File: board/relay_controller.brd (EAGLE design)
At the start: 75 x 50 mm, 73 parts, among them IC1 STM32F103C8T, IC3 AT24C, X1 RJ45-8L21-S, X2 RJ45-8L21-S

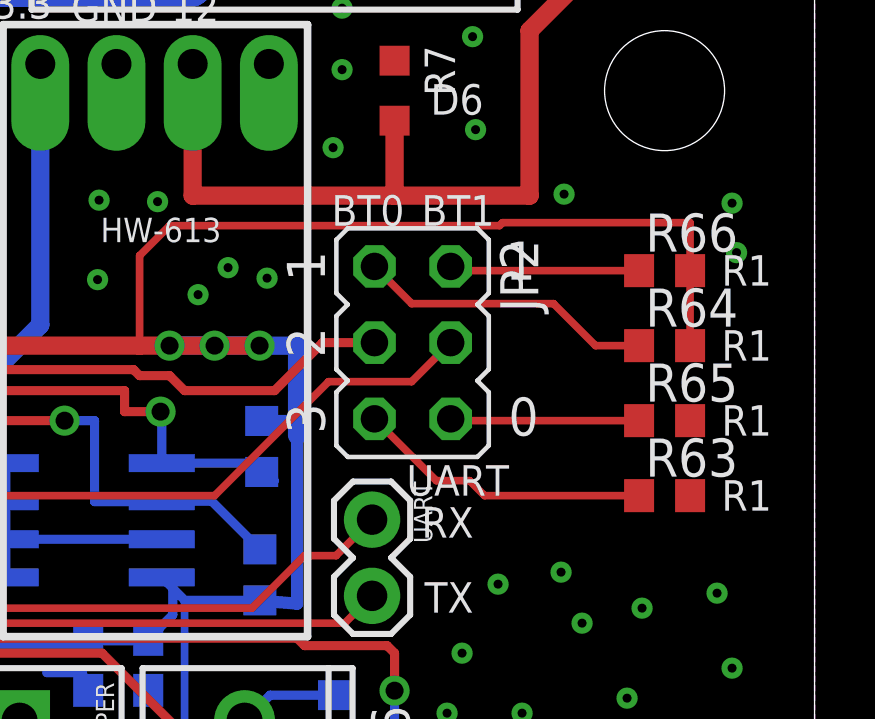
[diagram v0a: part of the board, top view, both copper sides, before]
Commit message: change to solderable boot jumper
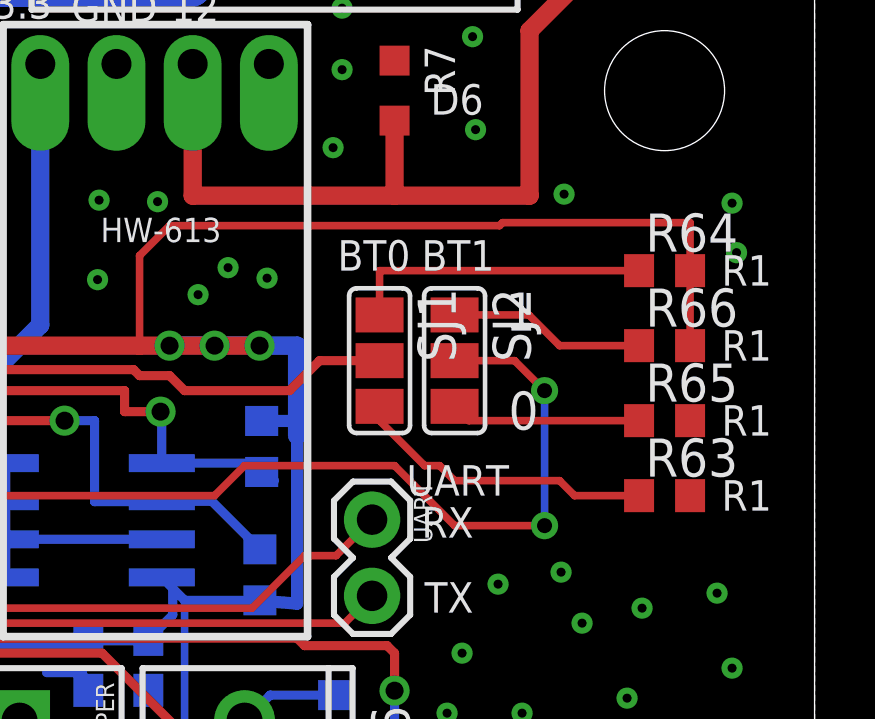
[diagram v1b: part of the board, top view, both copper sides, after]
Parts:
- removed JP2: (no value), jumper:JP3Q
- added SJ1, SJ2: (no value), jumper:SJ_2
- moved R64 2.50 mm to (70.0, 31.5)
- moved R66 2.50 mm to (70.0, 29.0)
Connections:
- net BOOT0: now also SJ1.2; no longer JP2.3
- net BOOT1: now also SJ2.2; no longer JP2.4
- net N$29: now also SJ2.1; no longer JP2.2
- net N$30: now also SJ1.1; no longer JP2.1
- net N$31: now also SJ2.3; no longer JP2.6
- net N$32: now also SJ1.3; no longer JP2.5
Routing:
- net BOOT1: track 46.0 -> 56.1 mm, vias 2 -> 4
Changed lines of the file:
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@@
 <text x="61.9" y="22.6" size="1.016" layer="121">RX</text>
 <text x="62" y="20.1" size="1.016" layer="121">TX</text>
-<text x="58.9" y="33" size="1.016" layer="121">BT0</text>
-<text x="61.9" y="33" size="1.016" layer="121">BT1</text>
-<text x="64.8" y="26" size="1.27" layer="121">0</text>
-<text x="64.7" y="31.2" size="1.27" layer="121">1</text>
+<text x="59.1" y="31.5" size="1.016" layer="121">BT0</text>
+<text x="61.9" y="31.5" size="1.016" layer="121">BT1</text>
+<text x="64.8" y="26.2" size="1.27" layer="121">0</text>
+<text x="64.7" y="29.5" size="1.27" layer="121">1</text>
 <text x="71.9" y="28.5" size="1.016" layer="121">R1</text>
 <text x="71.9" y="26" size="1.016" layer="121">R1</text>
@@
 <element name="U$5" library="mounting" package="C45-DIN-MOUNT-2-HOLE" value="" x="5" y="25"/>
 <element name="R63" library="rcl" package="R0603" value="10k" x="70" y="24"/>
-<element name="R64" library="rcl" package="R0603" value="10k" x="70" y="29"/>
+<element name="R64" library="rcl" package="R0603" value="10k" x="70" y="31.5"/>
 <element name="R65" library="rcl" package="R0603" value="10k" x="70" y="26.5"/>
-<element name="R66" library="rcl" package="R0603" value="10k" x="70" y="31.5"/>
-<element name="JP2" library="jumper" package="JP3Q" value="" x="61.6" y="29.1" rot="R270"/>
+<element name="R66" library="rcl" package="R0603" value="10k" x="70" y="29"/>
+<element name="SJ1" library="jumper" package="SJ_2" value="" x="60.5" y="28.5" rot="R270"/>
+<element name="SJ2" library="jumper" package="SJ_2" value="" x="63" y="28.5" rot="R270"/>
 </elements>
 <signals>
@@
 <wire x1="39.5" y1="24.5" x2="44.5" y2="24.5" width="0.6096" layer="16"/>
 <wire x1="44.5" y1="19" x2="44.5" y2="24.5" width="0.6096" layer="16"/>
-<wire x1="70.85" y1="29" x2="70.85" y2="31.5" width="0.254" layer="1"/>
 <wire x1="52.5" y1="29" x2="52.5" y2="32" width="0.254" layer="1"/>
 <wire x1="52.5" y1="32" x2="53.5" y2="33" width="0.254" layer="1"/>
@@
 <wire x1="64.6" y1="33.1" x2="70.85" y2="33.1" width="0.254" layer="1"/>
 <wire x1="70.85" y1="31.5" x2="70.85" y2="33.1" width="0.254" layer="1"/>
+<wire x1="70.85" y1="31.5" x2="70.85" y2="29" width="0.254" layer="1"/>
 </signal>
 <signal name="RELAY_16">
@@
 </signal>
 <signal name="BOOT1">
-<contactref element="JP2" pad="4"/>
 <contactref element="IC1" pad="20"/>
 <wire x1="32.75" y1="15.75" x2="32.75" y2="12.25" width="0.3048" layer="1"/>
 <wire x1="32.75" y1="12.25" x2="33.5" y2="11.5" width="0.3048" layer="1"/>
 <wire x1="33.5" y1="11.5" x2="40.1" y2="11.5" width="0.3048" layer="1"/>
-<wire x1="62.87" y1="29.1" x2="61.57" y2="27.8" width="0.254" layer="1"/>
-<wire x1="61.57" y1="27.8" x2="58.8" y2="27.8" width="0.254" layer="1"/>
-<wire x1="58.8" y1="27.8" x2="55" y2="24" width="0.254" layer="1"/>
 <wire x1="55" y1="24" x2="44.5" y2="24" width="0.254" layer="1"/>
 <wire x1="44.5" y1="24" x2="42.5" y2="22" width="0.254" layer="1"/>
@@
 <via x="40.9" y="12.3" extent="1-16" drill="0.5"/>
 <wire x1="40.9" y1="12.3" x2="40.1" y2="11.5" width="0.3048" layer="1"/>
+<contactref element="SJ2" pad="2"/>
+<wire x1="63" y1="28.5" x2="65" y2="28.5" width="0.254" layer="1"/>
+<wire x1="65" y1="28.5" x2="66" y2="27.5" width="0.254" layer="1"/>
+<via x="66" y="27.5" extent="1-16" drill="0.5"/>
+<wire x1="66" y1="27.5" x2="66" y2="23" width="0.254" layer="16"/>
+<via x="66" y="23" extent="1-16" drill="0.5"/>
+<wire x1="66" y1="23" x2="63" y2="23" width="0.254" layer="1"/>
+<wire x1="63" y1="23" x2="61" y2="25" width="0.254" layer="1"/>
+<wire x1="61" y1="25" x2="56" y2="25" width="0.254" layer="1"/>
+<wire x1="56" y1="25" x2="55" y2="24" width="0.254" layer="1"/>
 </signal>
 <signal name="BOOT0">
-<contactref element="JP2" pad="3"/>
 <contactref element="IC1" pad="44"/>
 <wire x1="31.25" y1="24.25" x2="31.25" y2="32.5" width="0.3048" layer="1"/>
@@
 <wire x1="52.5" y1="28" x2="53.5" y2="28" width="0.3048" layer="1"/>
 <wire x1="53.5" y1="28" x2="54" y2="27.5" width="0.3048" layer="1"/>
-<wire x1="54" y1="27.5" x2="57" y2="27.5" width="0.3048" layer="1"/>
-<wire x1="57" y1="27.5" x2="58.6" y2="29.1" width="0.3048" layer="1"/>
-<wire x1="58.6" y1="29.1" x2="60.33" y2="29.1" width="0.3048" layer="1"/>
+<wire x1="54" y1="27.5" x2="57.5" y2="27.5" width="0.3048" layer="1"/>
+<contactref element="SJ1" pad="2"/>
+<wire x1="57.5" y1="27.5" x2="58.5" y2="28.5" width="0.3048" layer="1"/>
+<wire x1="58.5" y1="28.5" x2="60.5" y2="28.5" width="0.3048" layer="1"/>
 </signal>
 <signal name="N$29">
 <contactref element="R66" pad="1"/>
-<contactref element="JP2" pad="2"/>
-<wire x1="62.87" y1="31.64" x2="63.01" y2="31.5" width="0.254" layer="1"/>
-<wire x1="63.01" y1="31.5" x2="69.15" y2="31.5" width="0.254" layer="1"/>
+<contactref element="SJ2" pad="1"/>
+<wire x1="63" y1="30.024" x2="65.476" y2="30.024" width="0.254" layer="1"/>
+<wire x1="65.476" y1="30.024" x2="66.5" y2="29" width="0.254" layer="1"/>
+<wire x1="66.5" y1="29" x2="69.15" y2="29" width="0.254" layer="1"/>
 </signal>
 <signal name="N$30">
 <contactref element="R64" pad="1"/>
-<contactref element="JP2" pad="1"/>
-<wire x1="60.33" y1="31.64" x2="61.57" y2="30.4" width="0.254" layer="1"/>
-<wire x1="61.57" y1="30.4" x2="66.3" y2="30.4" width="0.254" layer="1"/>
-<wire x1="66.3" y1="30.4" x2="67.7" y2="29" width="0.254" layer="1"/>
-<wire x1="67.7" y1="29" x2="69.15" y2="29" width="0.254" layer="1"/>
+<contactref element="SJ1" pad="1"/>
+<wire x1="60.5" y1="30.024" x2="60.5" y2="31.5" width="0.254" layer="1"/>
+<wire x1="60.5" y1="31.5" x2="69.15" y2="31.5" width="0.254" layer="1"/>
 </signal>
 <signal name="N$31">
 <contactref element="R65" pad="1"/>
-<contactref element="JP2" pad="6"/>
-<wire x1="62.87" y1="26.56" x2="62.93" y2="26.5" width="0.254" layer="1"/>
-<wire x1="62.93" y1="26.5" x2="69.15" y2="26.5" width="0.254" layer="1"/>
+<contactref element="SJ2" pad="3"/>
+<wire x1="69.15" y1="26.5" x2="63.476" y2="26.5" width="0.254" layer="1"/>
+<wire x1="63.476" y1="26.5" x2="63" y2="26.976" width="0.254" layer="1"/>
 </signal>
 <signal name="N$32">
 <contactref element="R63" pad="1"/>
-<contactref element="JP2" pad="5"/>
-<wire x1="60.33" y1="26.56" x2="62.39" y2="24.5" width="0.254" layer="1"/>
-<wire x1="62.39" y1="24.5" x2="63.5" y2="24.5" width="0.254" layer="1"/>
-<wire x1="63.5" y1="24.5" x2="64" y2="24" width="0.254" layer="1"/>
-<wire x1="64" y1="24" x2="69.15" y2="24" width="0.254" layer="1"/>
+<contactref element="SJ1" pad="3"/>
+<wire x1="69.15" y1="24" x2="67" y2="24" width="0.254" layer="1"/>
+<wire x1="67" y1="24" x2="66.5" y2="24.5" width="0.254" layer="1"/>
+<wire x1="66.5" y1="24.5" x2="63" y2="24.5" width="0.254" layer="1"/>
+<wire x1="63" y1="24.5" x2="62.5" y2="25" width="0.254" layer="1"/>
+<wire x1="62.5" y1="25" x2="62" y2="25" width="0.254" layer="1"/>
+<wire x1="62" y1="25" x2="60.5" y2="26.5" width="0.254" layer="1"/>
+<wire x1="60.5" y1="26.5" x2="60.5" y2="26.976" width="0.254" layer="1"/>
 </signal>
 </signals>

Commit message: value for current limiting resistor
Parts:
- R20: value (none) -> 100
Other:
- board text added: "R9"
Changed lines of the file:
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@@
 <text x="71.9" y="23.5" size="1.016" layer="121">R1</text>
 <text x="71.9" y="31" size="1.016" layer="121">R1</text>
+<text x="8.85" y="5.1" size="1.016" layer="122" rot="MR180">R9</text>
 </plain>
 <attributes>
@@
 <element name="R18" library="resistor" package="R0603" value="" x="29.8" y="4.5" rot="MR180"/>
 <element name="R19" library="resistor" package="R0603" value="" x="26.3" y="4.5" rot="MR180"/>
-<element name="R20" library="resistor" package="R0603" value="" x="12.3" y="4.5" rot="MR180"/>
+<element name="R20" library="resistor" package="R0603" value="100" x="12.3" y="4.5" rot="MR180"/>
 <element name="R21" library="resistor" package="R0603" value="" x="15.8" y="4.5" rot="MR0"/>
 <element name="R22" library="resistor" package="R0603" value="" x="22.8" y="4.5" rot="MR180"/>

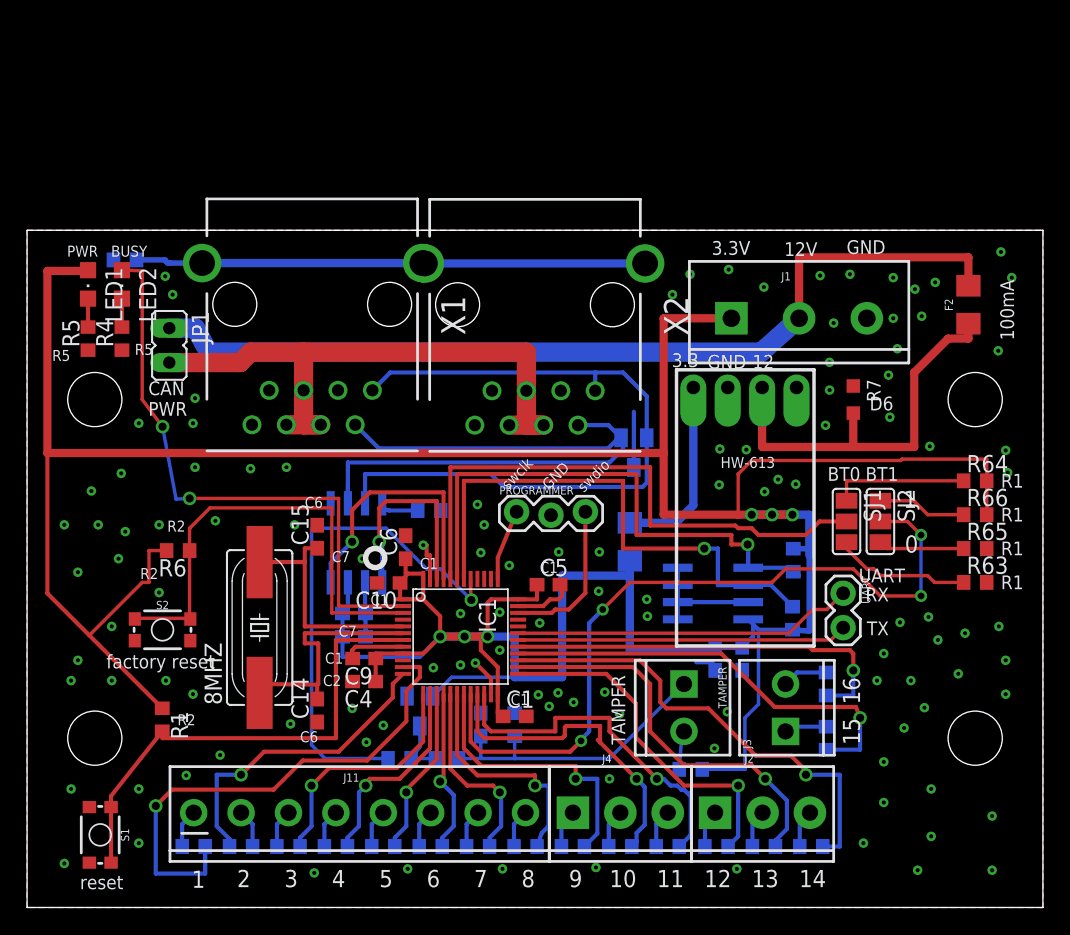
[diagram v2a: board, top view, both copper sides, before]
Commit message: change 16 driver pin to 5 relay output (g6k-2f-y)
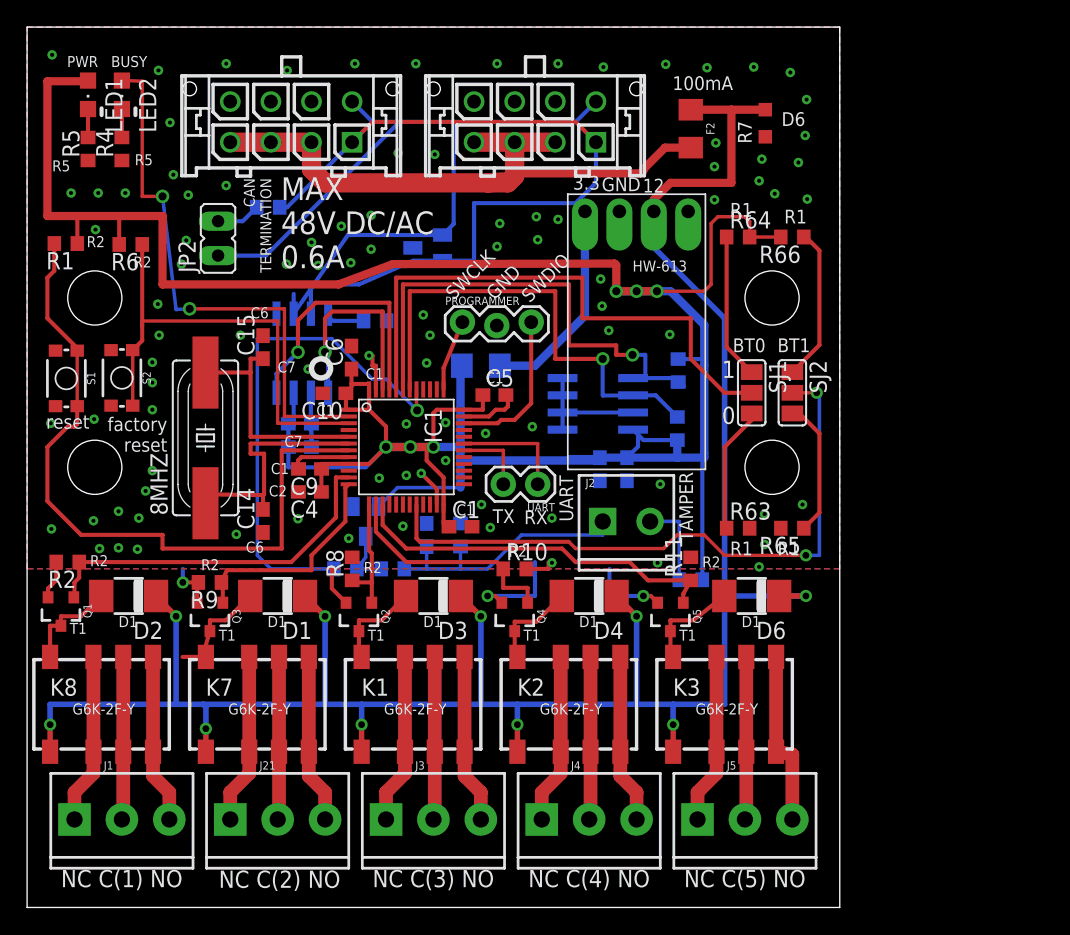
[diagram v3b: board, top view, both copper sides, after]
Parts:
- removed J11: (no value), SparkFun-Connectors:SCREWTERMINAL-3.5MM-8
- removed JP1: (no value), jumper:JP1
- removed R12, R13, R14, R15, R16, R17, R18, R19, R21, R22, R23: (no value), resistor:R0603
- removed R20: 100, resistor:R0603
- removed TAMPER: (no value), SparkFun-Connectors:SCREWTERMINAL-3.5MM-2
- removed U$4, U$5: (no value), mounting:C45-DIN-MOUNT-2-HOLE
- removed X1, X2: RJ45-8L21-S, con-tycoelectronics:RJ45-SHIELD1
- added D1, D2, D3, D4, D6: (no value), diode:DO-214AC
- added J21, J5: (no value), SparkFun-Connectors:SCREWTERMINAL-3.5MM-3
- added JP2: (no value), jumper:JP1
- added K1, K2, K3, K7, K8: G6K-2F-Y, relay:G6K-2F-Y
- added Q1, Q2, Q3, Q4, Q5: 220mA/50V/3.5Ω, SparkFun-DiscreteSemi:SOT23-3
- added R2: 10k, rcl:R0603
- added U$2, U$3: (no value), mounting:C45-DIN-MOUNT-2-HOLE-B
- added X3, X4: (no value), con-molex-micro-fit-3_0:43045-0812
- J1: device SparkFun-Connectors:SCREWTERMINAL-5MM-3 -> SparkFun-Connectors:SCREWTERMINAL-3.5MM-3
- J2: device SparkFun-Connectors:SCREWTERMINAL-3.5MM-3 -> SparkFun-Connectors:SCREWTERMINAL-3.5MM-2
- J3: device SparkFun-Connectors:SCREWTERMINAL-3.5MM-2 -> SparkFun-Connectors:SCREWTERMINAL-3.5MM-3
- R10, R11, R8, R9: value (none) -> 10k; device resistor:R0603 -> rcl:R0603
- R25: value 10k -> 120
- moved J1 61.0 mm to (3.50, 6.50)
- moved R9 46.9 mm to (13.5, 24.0), flipped to the top, turned to 180 degrees
- moved R8 36.0 mm to (24.0, 25.0), flipped to the top, turned to 90 degrees
- moved R1 35.9 mm to (2.86, 49.0), turned to 180 degrees
- moved S1 33.8 mm to (2.90, 39.1)
- moved J3 30.2 mm to (26.5, 6.50), turned to 0 degrees
- moved R10 30.0 mm to (36.0, 25.0), flipped to the top, turned to 0 degrees
- moved R64 25.1 mm to (52.5, 49.5)
- moved R66 24.5 mm to (56.5, 49.5), turned to 180 degrees
- moved F2 24.3 mm to (49.0, 57.5), turned to 270 degrees
- moved UART 23.9 mm to (37.7, 31.2), turned to 180 degrees
- moved J2 23.0 mm to (42.5, 28.5)
- moved R6 22.9 mm to (7.65, 49.0)
- moved D5 21.5 mm to (29.6, 48.7), turned to 270 degrees
- moved R7 21.4 mm to (54.5, 57.9), turned to 90 degrees
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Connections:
- removed net N$20: R25.1, X1.S1, X1.S2, X2.S1, X2.S2
- removed net RELAY_10: IC1.21, R14.2
- removed net RELAY_11: IC1.22, R13.2
- removed net RELAY_13: IC1.26, R11.2
- removed net RELAY_14: IC1.27, R10.2
- removed net RELAY_15: IC1.28, R9.2
- removed net RJ45_12V: JP1.2, X1.4, X1.5, X1.6, X2.4, X2.5, X2.6
- new net N$12: JP2.2, R25.1
- new net N$33: J5.1, K3.2, K3.7
- new net N$34: J5.3, K3.4, K3.5
- new net N$35: J5.2, K3.3, K3.6
- new net N$36: D6.A, K3.8, Q5.3
- net +12V: now also D1.C, D2.C, D3.C, D4.C, D6.C, K1.1, K2.1, K3.1, K7.1, K8.1
- net +3V3: no longer J1.1
- net CAN_H: now also R25.2, X3.P$1, X4.P$1; no longer X1.1, X2.1
- net CAN_L: now also JP2.1, X3.P$5, X4.P$5; no longer X1.2, X2.2
- net GND: now also Q1.2, Q2.2, Q3.2, Q4.2, Q5.2, R10.2, R11.2, R2.2, R8.2, R9.2, X3.P$6, X3.P$7, X3.P$8, X4.P$6, X4.P$7, X4.P$8; no longer J1.3, R25.2, X1.3, X1.7, X1.8, X2.3, X2.7, X2.8
- net N$10: now also J2.2; no longer TAMPER.2
- net N$13: now also J21.3, K7.4, K7.5; no longer J2.3, R10.1
- net N$14: now also J21.2, K7.3, K7.6; no longer J2.2, R11.1
- net N$15: now also D1.A, K7.8, Q3.3; no longer J2.1, R12.1
- net N$16: now also J1.3, K8.4, K8.5; no longer J4.3, R13.1
- net N$18: now also J1.2, K8.3, K8.6; no longer J4.2, R14.1
- net N$19: now also D2.A, K8.8, Q1.3; no longer J4.1, R15.1
- net N$21: now also J3.1, K1.2, K1.7; no longer J11.8, R16.1
- net N$22: now also J3.3, K1.4, K1.5; no longer J11.7, R17.1
- net N$23: now also J3.2, K1.3, K1.6; no longer J11.6, R18.1
- net N$24: now also D3.A, K1.8, Q2.3; no longer J11.5, R19.1
- net N$25: now also J4.1, K2.2, K2.7; no longer J11.1, R20.1
- net N$26: now also J4.3, K2.4, K2.5; no longer J11.2, R21.1
- net N$27: now also J4.2, K2.3, K2.6; no longer J11.4, R22.1
- net N$28: now also D4.A, K2.8, Q4.3; no longer J11.3, R23.1
- net N$4: now also J21.1, K7.2, K7.7; no longer J3.2, R8.1
- net N$5: now also J2.1; no longer TAMPER.1
- net N$9: now also J1.1, K8.2, K8.7; no longer J3.1, R9.1
- net PRE_FUSE_12V: now also X3.P$2, X3.P$3, X3.P$4, X4.P$2, X4.P$3, X4.P$4; no longer J1.2, JP1.1
- net RELAY_1: now also Q1.1, R2.1; no longer R20.2
- net RELAY_12: no longer R12.2
- net RELAY_16: no longer R8.2
- net RELAY_2: now also Q3.1, R9.1; no longer R21.2
- net RELAY_3: now also Q2.1, R8.1; no longer R23.2
- net RELAY_4: now also Q4.1, R10.1; no longer R22.2
- net RELAY_5: now also Q5.1, R11.1; no longer R19.2
- net RELAY_6: no longer R18.2
- net RELAY_7: no longer R17.2
- net RELAY_8: no longer R16.2
- net RELAY_9: no longer R15.2
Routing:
- net +12V: track 29.8 -> 166.4 mm, vias 0 -> 10
- net +3V3: track 285.2 -> 212.6 mm
- net RJ45_12V: track 45.1 -> 0.00 mm
- net N$20: track 37.7 -> 0.00 mm
- net RELAY_14: track 34.9 -> 0.00 mm, vias 1 -> 0
- net RELAY_15: track 32.3 -> 0.00 mm, vias 1 -> 0
- net RELAY_16: track 30.1 -> 0.00 mm, vias 1 -> 0
- net RELAY_13: track 29.7 -> 0.00 mm, vias 1 -> 0
- net RELAY_11: track 26.0 -> 0.00 mm, vias 1 -> 0
- net RELAY_12: track 25.9 -> 0.00 mm, vias 1 -> 0
- net RELAY_10: track 23.6 -> 0.00 mm, vias 1 -> 0
- net RELAY_9: track 20.7 -> 0.00 mm, vias 1 -> 0
- net PRE_FUSE_12V: track 67.6 -> 47.8 mm
- net UART_TX: track 24.4 -> 5.41 mm
- net GND: track 35.1 -> 53.9 mm, vias 118 -> 98
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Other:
- board size 75 x 50 mm -> 60 x 65 mm
- board text added: "CAN TERMINATION"
- board text added: "D1"
- board text added: "G6K-2F-Y"
- board text added: "MAX 48V DC/AC 0.6A"
- board text added: "NC C(1) NO"
- board text added: "NC C(2) NO"
- board text added: "NC C(3) NO"
- board text added: "NC C(4) NO"
- board text added: "NC C(5) NO"
- board text added: "R21"
- board text added: "SWCLK"
- board text added: "SWDIO"
- board text added: "T1"
- board text added: "relay controller 2020.11.22 v1.3"
- board text removed: "10"
- board text removed: "11"
- board text removed: "12V"
- board text removed: "13"
- board text removed: "14"
- board text removed: "15"
- board text removed: "16"
- board text removed: "2"
- board text removed: "3"
- board text removed: "3.3V"
- board text removed: "4"
- board text removed: "5"
- board text removed: "6"
- board text removed: "7"
- board text removed: "8"
- board text removed: "9"
- board text removed: "CAN PWR"
- board text removed: "R9"
- board text removed: "SHIELD"
- board text removed: "relay controller 2020.07.18 v1.1"
- board text removed: "shield"
- board text removed: "swclk"
- board text removed: "swdio"
